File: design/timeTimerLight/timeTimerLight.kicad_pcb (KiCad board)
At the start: 2 copper layers, 50.8 x 25.4 mm, 13 parts, among them J1 640455-3, Q1 2N3906, U1 MCP1640x-xCHY

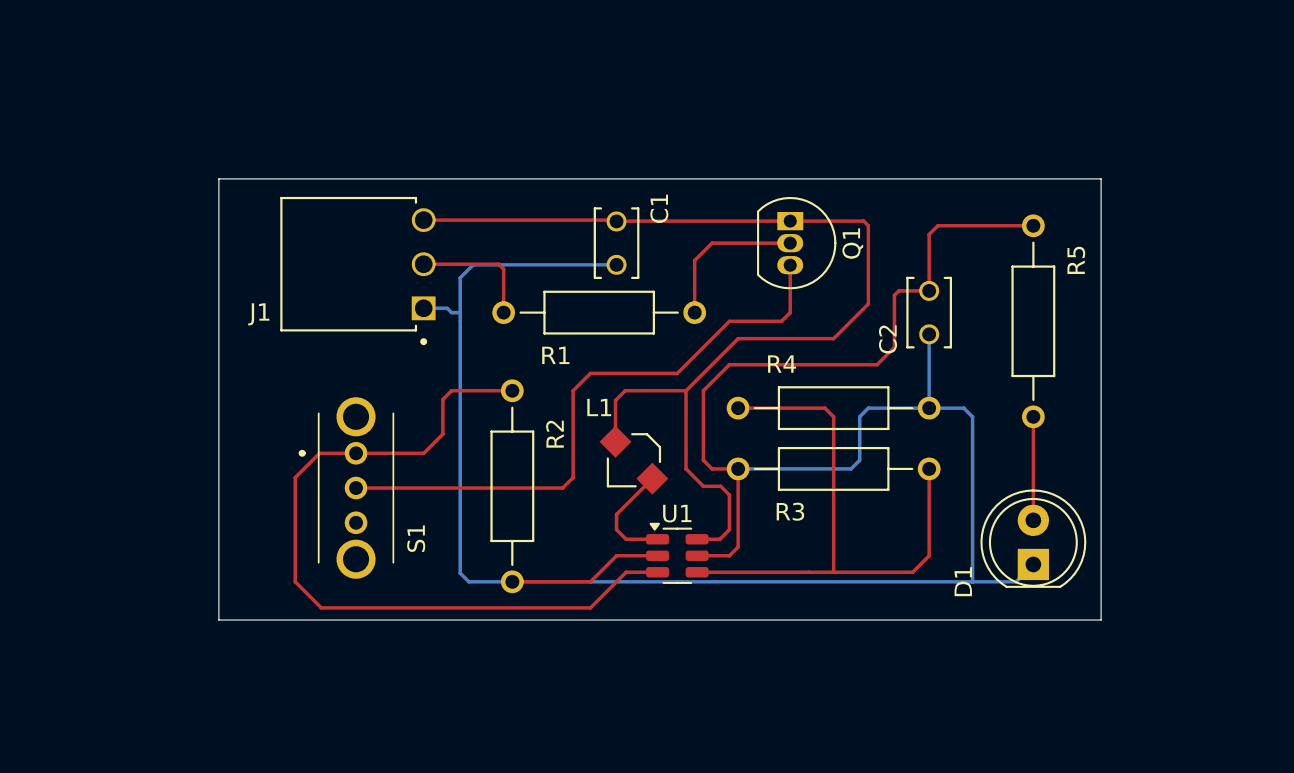
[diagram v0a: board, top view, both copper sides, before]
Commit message: Fixed some traces.  Moved part descriptions to main silk layer.
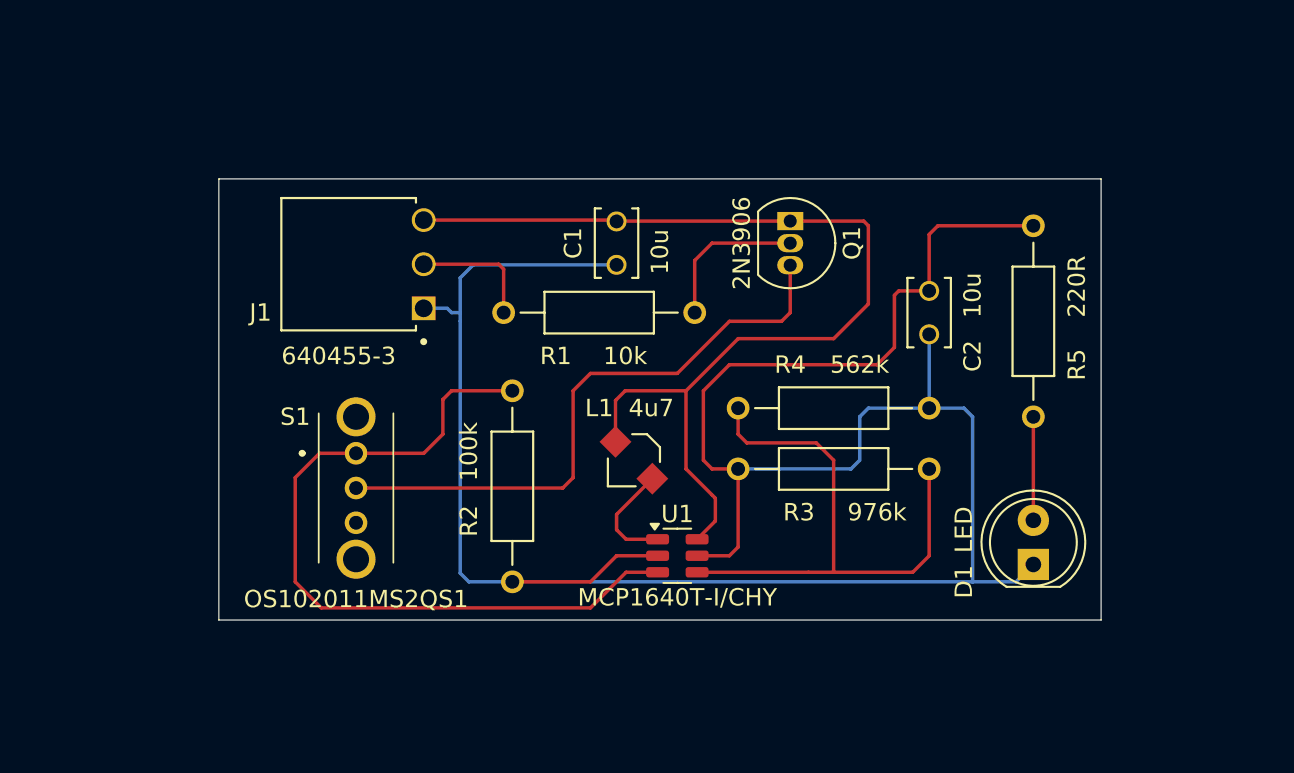
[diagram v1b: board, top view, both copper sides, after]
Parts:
- U1: value MCP1640x-xCHY -> MCP1640T-I/CHY
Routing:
- net /+1V2: track 61.2 -> 59.2 mm
- net Net-(U1-V_{FB}): track 33.4 -> 32.8 mm
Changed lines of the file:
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@@
 		(at 156.5 120.5 90)
 		(property "Reference" "C2"
-			(at -1.51934 -2.335 90)
+			(at -2.5 2.5 90)
 			(layer "F.SilkS")
 			(effects
@@
 		)
 		(property "Value" "10u"
-			(at 1.48066 -2.37934 90)
-			(layer "F.Fab")
+			(at 1 2.5 90)
+			(layer "F.SilkS")
 			(effects
 				(font
@@
 		(at 151 126)
 		(property "Reference" "R4"
-			(at -3 -2.5 0)
+			(at -2.5 -2.5 0)
 			(layer "F.SilkS")
 			(effects
@@
 		)
 		(property "Value" "562k"
-			(at 0.5 -2.5 0)
-			(layer "F.Fab")
+			(at 1.5 -2.5 0)
+			(layer "F.SilkS")
 			(effects
 				(font
@@
 		(property "Value" "640455-3"
 			(at 2.7475 4.895 0)
-			(layer "F.Fab")
+			(layer "F.SilkS")
 			(effects
 				(font
@@
 			)
 		)
-		(property "Value" "MCP1640x-xCHY"
+		(property "Value" "MCP1640T-I/CHY"
 			(at 0 2.4 0)
-			(layer "F.Fab")
+			(layer "F.SilkS")
 			(effects
 				(font
@@
 		(at 132.5 130.5 -90)
 		(property "Reference" "R2"
-			(at -3 -2.5 90)
+			(at 2 2.5 90)
 			(layer "F.SilkS")
 			(effects
@@
 		)
 		(property "Value" "100k"
-			(at 1 -2.5 90)
-			(layer "F.Fab")
+			(at -2 2.5 90)
+			(layer "F.SilkS")
 			(effects
 				(font
@@
 		(property "Value" "2N3906"
 			(at 1.27 2.79 90)
-			(layer "F.Fab")
+			(layer "F.SilkS")
 			(effects
 				(font
@@
 		(descr "<b>OS102011MS2QS1-2</b><br>")
 		(property "Reference" "S1"
-			(at 4.9 -3.5 90)
+			(at -2.1 3.5 0)
 			(layer "F.SilkS")
 			(effects
@@
 		)
 		(property "Value" "OS102011MS2QS1"
-			(at 2.4 5.605 90)
-			(layer "F.Fab")
+			(at 8.4 0 180)
+			(layer "F.SilkS")
 			(effects
 				(font
@@
 		)
 		(property "Value" "10k"
-			(at -1 -2.5 0)
-			(layer "F.Fab")
+			(at -1.5 -2.5 0)
+			(layer "F.SilkS")
 			(effects
 				(font
@@
 		(at 138.5 116.5 -90)
 		(property "Reference" "C1"
-			(at -2 -2.5 90)
+			(at 0 2.5 90)
 			(layer "F.SilkS")
 			(effects
@@
 		)
 		(property "Value" "10u"
-			(at 1 -2.5 90)
-			(layer "F.Fab")
+			(at 0.5 -2.5 90)
+			(layer "F.SilkS")
 			(effects
 				(font
@@
 		(property "Value" "4u7"
 			(at 1 -3 0)
-			(layer "F.Fab")
+			(layer "F.SilkS")
 			(effects
 				(font
@@
 		(at 151 129.5)
 		(property "Reference" "R3"
-			(at -2.5 2.5 0)
+			(at -2 2.5 0)
 			(layer "F.SilkS")
 			(effects
@@
 		)
 		(property "Value" "976k"
-			(at 1 2.5 0)
-			(layer "F.Fab")
+			(at 2.5 2.5 0)
+			(layer "F.SilkS")
 			(effects
 				(font
@@
 		(property "Value" "LED"
 			(at 2 -4 90)
-			(layer "F.Fab")
+			(layer "F.SilkS")
 			(effects
 				(font
@@
 		(at 162.5 121 -90)
 		(property "Reference" "R5"
-			(at -3.5 -2.5 90)
+			(at 2.5 -2.5 90)
 			(layer "F.SilkS")
 			(effects
@@
 		)
 		(property "Value" "220R"
-			(at 0.5 -2.5 90)
-			(layer "F.Fab")
+			(at -2 -2.5 90)
+			(layer "F.SilkS")
 			(effects
 				(font
@@
 	)
 	(segment
-		(start 145 131)
-		(end 144.5 130.5)
+		(start 148.5 115.23)
+		(end 152.73 115.23)
 		(width 0.2)
 		(layer "F.Cu")
@@
 	)
 	(segment
-		(start 148.5 115.23)
-		(end 152.73 115.23)
+		(start 138.4225 115.1725)
+		(end 138.5 115.25)
 		(width 0.2)
 		(layer "F.Cu")
@@
 	)
 	(segment
-		(start 138.4225 115.1725)
-		(end 138.5 115.25)
+		(start 143.1375 133.55)
+		(end 144.1875 132.5)
 		(width 0.2)
 		(layer "F.Cu")
@@
 	)
 	(segment
-		(start 138.43934 125.56066)
-		(end 138.43934 127.93934)
+		(start 144 131)
+		(end 142.5 129.5)
 		(width 0.2)
 		(layer "F.Cu")
@@
 	)
 	(segment
-		(start 152.73 115.23)
-		(end 153 115.5)
+		(start 144.1875 132.5)
+		(end 144.1875 131.1875)
 		(width 0.2)
 		(layer "F.Cu")
@@
 	)
 	(segment
-		(start 145 133)
-		(end 145 131)
+		(start 138.43934 125.56066)
+		(end 138.43934 127.93934)
 		(width 0.2)
 		(layer "F.Cu")
@@
 	)
 	(segment
-		(start 153 115.5)
-		(end 153 120)
+		(start 152.73 115.23)
+		(end 153 115.5)
 		(width 0.2)
 		(layer "F.Cu")
@@
 	)
 	(segment
-		(start 143.1375 133.55)
-		(end 144.45 133.55)
+		(start 153 115.5)
+		(end 153 120)
 		(width 0.2)
 		(layer "F.Cu")
@@
 	)
 	(segment
-		(start 144.45 133.55)
-		(end 145 133)
+		(start 142.5 129.5)
+		(end 142.5 125)
 		(width 0.2)
 		(layer "F.Cu")
@@
 	)
 	(segment
-		(start 144.5 130.5)
-		(end 143.5 130.5)
-		(width 0.2)
-		(layer "F.Cu")
-		(net 1)
-	)
-	(segment
 		(start 142.5 125)
 		(end 139 125)
@@
 	)
 	(segment
-		(start 153 120)
-		(end 151 122)
+		(start 144.1875 131.1875)
+		(end 144 131)
 		(width 0.2)
 		(layer "F.Cu")
@@
 	)
 	(segment
-		(start 145.5 122)
-		(end 142.5 125)
+		(start 153 120)
+		(end 151 122)
 		(width 0.2)
 		(layer "F.Cu")
@@
 	)
 	(segment
-		(start 142.5 129.5)
+		(start 145.5 122)
 		(end 142.5 125)
 		(width 0.2)
@@
 	)
 	(segment
-		(start 143.5 130.5)
-		(end 142.5 129.5)
-		(width 0.2)
-		(layer "F.Cu")
-		(net 1)
-	)
-	(segment
 		(start 154.75 119.25)
 		(end 156.5 119.25)
@@
 	)
 	(segment
-		(start 150.5 126)
-		(end 151 126.5)
+		(start 146 128)
+		(end 150 128)
+		(width 0.2)
+		(layer "F.Cu")
+		(net 9)
+	)
+	(segment
+		(start 145.5 126)
+		(end 145.5 127.5)
 		(width 0.2)
 		(layer "F.Cu")
@@
 	)
 	(segment
+		(start 150 128)
+		(end 151 129)
+		(width 0.2)
+		(layer "F.Cu")
+		(net 9)
+	)
+	(segment
 		(start 156.5 134.5)
 		(end 156.5 129.5)
@@
 	)
 	(segment
-		(start 149.55 135.45)
-		(end 151 135.45)
+		(start 145.5 127.5)
+		(end 146 128)
 		(width 0.2)
 		(layer "F.Cu")
@@
 	)
 	(segment
-		(start 151 126.5)
+		(start 149.55 135.45)
 		(end 151 135.45)
 		(width 0.2)
@@
 	)
 	(segment
-		(start 145.5 126)
-		(end 150.5 126)
+		(start 151 129)
+		(end 151 135.45)
 		(width 0.2)
 		(layer "F.Cu")

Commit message: Added board name, version number, author.
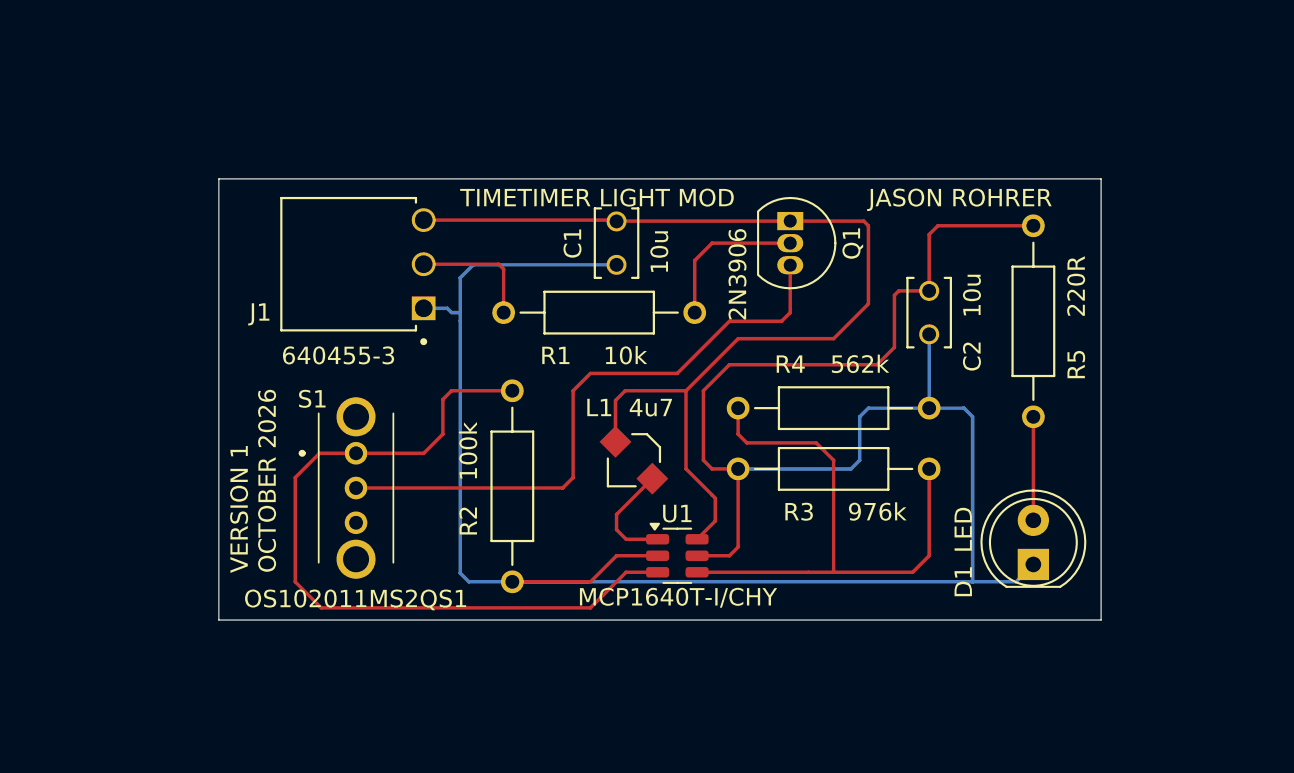
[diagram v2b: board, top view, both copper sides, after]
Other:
- board text added: "JASON ROHRER"
- board text added: "TIMETIMER LIGHT MOD"
- board text added: "VERSION 1 OCTOBER 2026"
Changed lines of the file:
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@@
 		)
 		(property "Value" "2N3906"
-			(at 1.27 2.79 90)
+			(at 3.07 3 90)
 			(layer "F.SilkS")
 			(effects
@@
 		(descr "<b>OS102011MS2QS1-2</b><br>")
 		(property "Reference" "S1"
-			(at -2.1 3.5 0)
+			(at -3.1 2.5 0)
 			(layer "F.SilkS")
 			(effects
@@
 		(layer "Edge.Cuts")
 	)
+	(gr_text "TIMETIMER LIGHT MOD"
+		(at 129.5 114.5 0)
+		(layer "F.SilkS")
+		(effects
+			(font
+				(size 1 1)
+				(thickness 0.1)
+			)
+			(justify left bottom)
+		)
+	)
+	(gr_text "JASON ROHRER"
+		(at 153 114.5 0)
+		(layer "F.SilkS")
+		(effects
+			(font
+				(size 1 1)
+				(thickness 0.1)
+			)
+			(justify left bottom)
+		)
+	)
+	(gr_text "VERSION 1\nOCTOBER 2026"
+		(at 119 135.5 90)
+		(layer "F.SilkS")
+		(effects
+			(font
+				(size 1 1)
+				(thickness 0.1)
+			)
+			(justify left bottom)
+		)
+	)
 	(segment

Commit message: Fixed Time Timer name to have space.
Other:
- board text added: "TIME TIMER LIGHT MOD"
- board text removed: "TIMETIMER LIGHT MOD"
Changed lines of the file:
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@@
 		(layer "Edge.Cuts")
 	)
-	(gr_text "TIMETIMER LIGHT MOD"
-		(at 129.5 114.5 0)
+	(gr_text "TIME TIMER LIGHT MOD"
+		(at 129 114.5 0)
 		(layer "F.SilkS")
 		(effects

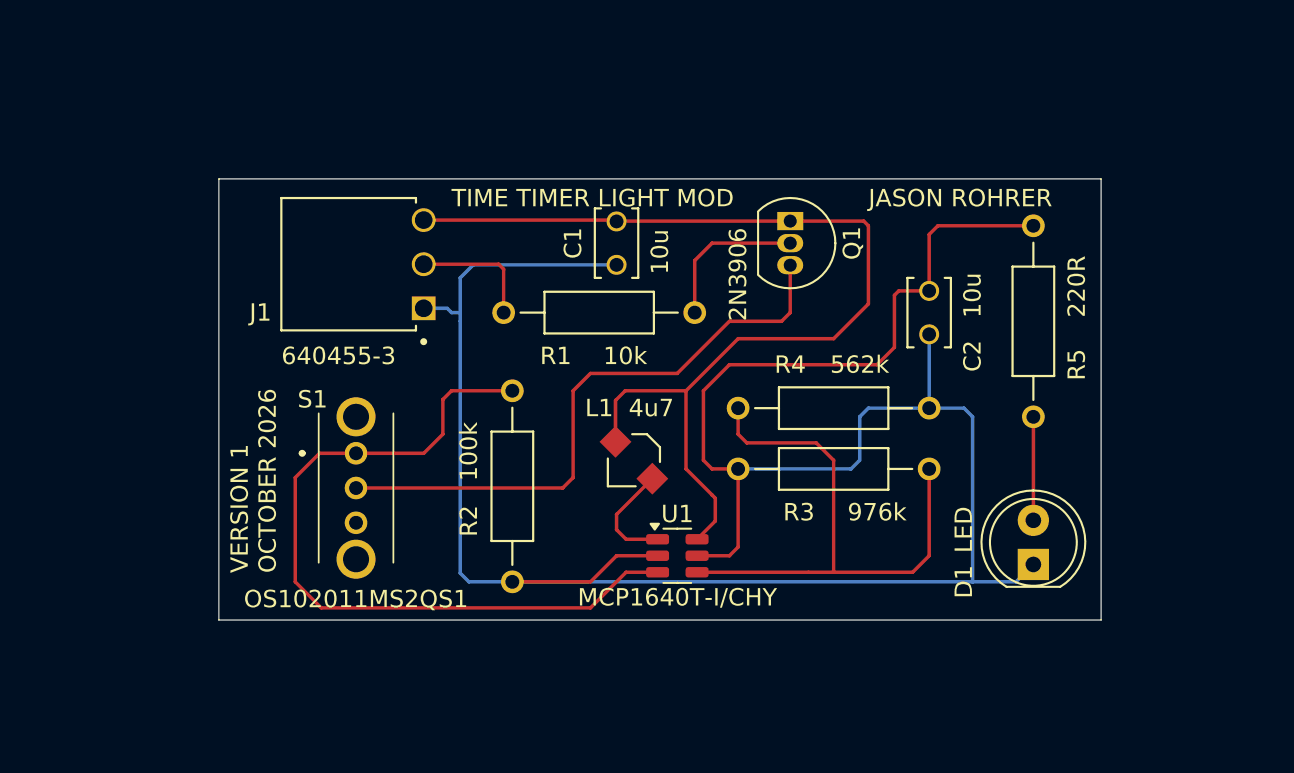
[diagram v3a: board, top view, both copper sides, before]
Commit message: Whoops, original schematic had a short circuit to ground on Vout 3.3v.  Breadboard prototype did not have this, but fixed it in schematic and PCB... Close call!
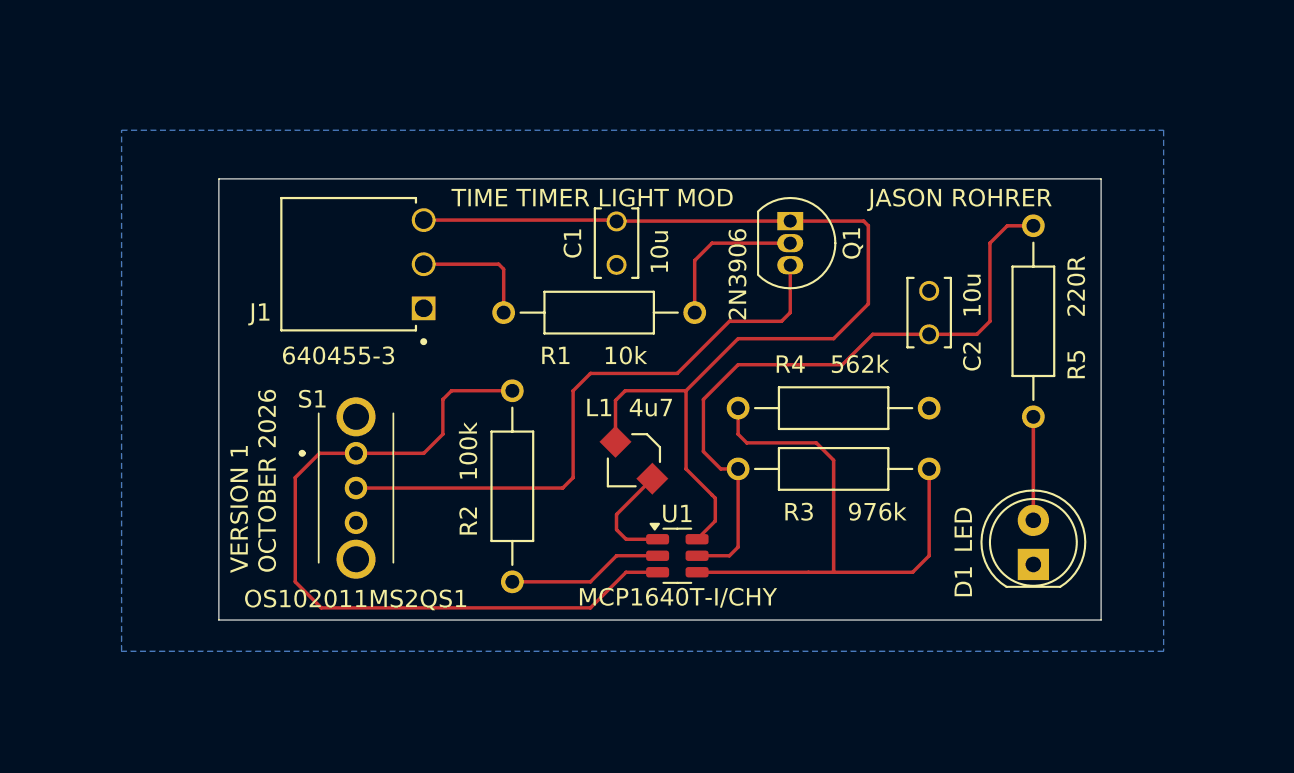
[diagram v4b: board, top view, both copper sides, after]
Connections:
- C2 pad 1: GND1 -> /+3V3
- R3 pad 1: GND1 -> /+3V3
- R5 pad 1: GND1 -> /+3V3
- U1 pad 5: GND1 -> /+3V3
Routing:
- net GND1: track 138.9 -> 8.98 mm
- net /+3V3: track 0.00 -> 38.3 mm
- added copper zone on B.Cu, net GND1

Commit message: Added screw mounting holes.
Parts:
- added REF**: MountingHole_2.2mm_M2_ISO7380, MountingHole:MountingHole_2.2mm_M2_ISO7380, F.Cu at (153.5, 135.5)
- added REF**: MountingHole_2.2mm_M2_ISO7380, MountingHole:MountingHole_2.2mm_M2_ISO7380, F.Cu at (157.0, 116.0)
- added REF**: MountingHole_2.2mm_M2_ISO7380, MountingHole:MountingHole_2.2mm_M2_ISO7380, F.Cu at (128.5, 124.5)
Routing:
- net Net-(S1-NO): track 44.1 -> 49.4 mm
- net Net-(U1-V_{FB}): track 32.8 -> 28.0 mm
